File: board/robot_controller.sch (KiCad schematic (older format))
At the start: 3 parts

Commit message: Voltage Regulator, Reset Logic
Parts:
- added C?: 100nF, symbol CAP
- added C? (x2): 2.2uF, symbol C
- added SW?: SPST, symbol SPST
- gave numbers to parts that had none: 3
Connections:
- net at U2.106 (VCAP2): now also C?.2
- net +3.3V: now reaches U2.108 (VDD)
- net +3.3V: now also U2.121 (VDD), U2.131 (VDD), U2.144 (VDD), U2.17 (VDD), U2.30 (VDD), U2.32 (VREF+), U2.33 (VDDA), U2.39 (VDD), U2.52 (VDD), U2.6 (VBAT), U2.62 (VDD), U2.72 (VDD), U2.84 (VDD), U2.95 (VDD)
- net MCU_RESET: now reaches U2.25 (~NRST)
- net MCU_RESET: now also C?.1, SW?.1
- net at U2.71 (VCAP1): now also C?.2
- new net GND: C?.1, C?.1, C?.2, SW?.2
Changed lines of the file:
@@
 $EndDescr
 $Comp
-L STM32F405-144 U?
+L STM32F405-144 U2
 U 1 1 52E41F67
 P 37850 17150
-F 0 "U?" H 36350 13600 60  0000 C CNN
+F 0 "U2" H 36350 13600 60  0000 C CNN
 F 1 "STM32F405-144" H 37850 17150 60  0000 C CNN
 F 2 "" H 35850 14500 60  0000 C CNN
@@
 $EndComp
 $Comp
-L L6470 U?
+L L6470 U1
 U 1 1 52E4501F
 P 3950 4400
-F 0 "U?" H 3300 3450 60  0000 C CNN
+F 0 "U1" H 3300 3450 60  0000 C CNN
 F 1 "L6470" H 3950 4400 60  0000 C CNN
 F 2 "" H 5000 4200 60  0000 C CNN
@@
 $EndComp
 $Comp
-L CONN_STEPPER J?
+L CONN_STEPPER J1
 U 1 1 52E45532
 P 5525 4400
-F 0 "J?" H 5425 4050 60  0000 C CNN
+F 0 "J1" H 5425 4050 60  0000 C CNN
 F 1 "CONN_STEPPER" V 5775 4400 60  0001 C CNN
 F 2 "" H 5075 4200 60  0000 C CNN
@@
 	1    0    0    -1
 $EndComp
+$Comp
+L GND #PWR01
+U 1 1 52E46471
+P 36000 13450
+F 0 "#PWR01" H 36000 13450 30  0001 C CNN
+F 1 "GND" H 36000 13380 30  0001 C CNN
+F 2 "" H 36000 13450 60  0000 C CNN
+F 3 "" H 36000 13450 60  0000 C CNN
+	1    36000 13450
+	1    0    0    -1
+$EndComp
+Connection ~ 36000 13250
+Wire Wire Line
+	36000 13250 36150 13250
+Wire Wire Line
+	36000 12850 36000 13450
+Wire Wire Line
+	36000 12850 36150 12850
+Wire Wire Line
+	36800 12850 36800 13350
+Wire Wire Line
+	36550 12850 36800 12850
+Wire Wire Line
+	36700 13250 36700 13350
+Wire Wire Line
+	36550 13250 36700 13250
+Text Label 38800 13250 1    60   ~ 0
+MCU_RESET
+Wire Wire Line
+	38800 13250 38800 13350
+Wire Wire Line
+	40600 12900 40800 12900
+Text Label 40600 12900 2    60   ~ 0
+MCU_RESET
+$Comp
+L CAP C?
+U 1 1 52E46E20
+P 40700 13250
+F 0 "C?" H 40800 13400 50  0000 C CNN
+F 1 "100nF" H 40850 13100 50  0000 C CNN
+F 2 "" H 40700 13250 60  0000 C CNN
+F 3 "" H 40700 13250 60  0000 C CNN
+	1    40700 13250
+	1    0    0    -1
+$EndComp
+$Comp
+L GND #PWR?
+U 1 1 52E46E34
+P 40700 13600
+F 0 "#PWR?" H 40700 13600 30  0001 C CNN
+F 1 "GND" H 40700 13530 30  0001 C CNN
+F 2 "" H 40700 13600 60  0000 C CNN
+F 3 "" H 40700 13600 60  0000 C CNN
+	1    40700 13600
+	1    0    0    -1
+$EndComp
+Wire Wire Line
+	40700 13500 40700 13600
+Wire Wire Line
+	40700 12900 40700 13000
+$Comp
+L SPST SW?
+U 1 1 52E4700C
+P 41300 12900
+F 0 "SW?" H 41300 13000 70  0000 C CNN
+F 1 "SPST" H 41300 12800 70  0000 C CNN
+F 2 "" H 41300 12900 60  0000 C CNN
+F 3 "" H 41300 12900 60  0000 C CNN
+	1    41300 12900
+	1    0    0    -1
+$EndComp
+Connection ~ 40700 12900
+$Comp
+L GND #PWR?
+U 1 1 52E4704D
+P 41900 13000
+F 0 "#PWR?" H 41900 13000 30  0001 C CNN
+F 1 "GND" H 41900 12930 30  0001 C CNN
+F 2 "" H 41900 13000 60  0000 C CNN
+F 3 "" H 41900 13000 60  0000 C CNN
+	1    41900 13000
+	1    0    0    -1
+$EndComp
+Wire Wire Line
+	41800 12900 41900 12900
+Wire Wire Line
+	41900 12900 41900 13000
+$Comp
+L +3.3V #PWR?
+U 1 1 52E474FF
+P 37000 13150
+F 0 "#PWR?" H 37000 13110 30  0001 C CNN
+F 1 "+3.3V" H 37000 13260 30  0000 C CNN
+F 2 "" H 37000 13150 60  0000 C CNN
+F 3 "" H 37000 13150 60  0000 C CNN
+	1    37000 13150
+	1    0    0    -1
+$EndComp
+Wire Wire Line
+	37000 13150 37000 13350
+Wire Wire Line
+	37000 13250 38600 13250
+Wire Wire Line
+	38600 13250 38600 13350
+Connection ~ 37000 13250
+Wire Wire Line
+	38300 13350 38300 13250
+Connection ~ 38300 13250
+Wire Wire Line
+	38200 13350 38200 13250
+Connection ~ 38200 13250
+Wire Wire Line
+	38100 13350 38100 13250
+Connection ~ 38100 13250
+Wire Wire Line
+	38000 13350 38000 13250
+Connection ~ 38000 13250
+Wire Wire Line
+	37900 13250 37900 13350
+Connection ~ 37900 13250
+Wire Wire Line
+	37800 13250 37800 13350
+Connection ~ 37800 13250
+Wire Wire Line
+	37700 13350 37700 13250
+Connection ~ 37700 13250
+Wire Wire Line
+	37600 13350 37600 13250
+Connection ~ 37600 13250
+Wire Wire Line
+	37500 13350 37500 13250
+Connection ~ 37500 13250
+Wire Wire Line
+	37400 13350 37400 13250
+Connection ~ 37400 13250
+Wire Wire Line
+	37300 13350 37300 13250
+Connection ~ 37300 13250
+Wire Wire Line
+	37200 13250 37200 13350
+Connection ~ 37200 13250
+Wire Wire Line
+	38500 13350 38500 13250
+Connection ~ 38500 13250
+$Comp
+L C C?
+U 1 1 52E477FB
+P 36350 13250
+F 0 "C?" V 36300 13150 50  0000 R CNN
+F 1 "2.2uF" V 36450 13150 50  0000 R CNN
+F 2 "" H 36350 13250 60  0000 C CNN
+F 3 "" H 36350 13250 60  0000 C CNN
+	1    36350 13250
+	0    -1   -1   0
+$EndComp
+$Comp
+L C C?
+U 1 1 52E478D0
+P 36350 12850
+F 0 "C?" V 36300 12750 50  0000 R CNN
+F 1 "2.2uF" V 36450 12750 50  0000 R CNN
+F 2 "" H 36350 12850 60  0000 C CNN
+F 3 "" H 36350 12850 60  0000 C CNN
+	1    36350 12850
+	0    -1   -1   0
+$EndComp
 $EndSCHEMATC

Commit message: Wired up the stepper driver blocks in the main schematic.
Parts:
- removed J1: CONN_STEPPER, symbol CONN_STEPPER
- removed U1: L6470, symbol L6470
- added R?: 1.1k, symbol R
- added R?: 16k, symbol R
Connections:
- net labels added: +24V, 24V_ADC, MISO, MOSI, SCK, STEPPER0-~CS, STEPPER0_~BUSY~/SYNC, STEPPER1-~CS, STEPPER1_~BUSY~/SYNC, STEPPER2-~CS, STEPPER2_~BUSY~/SYNC, STEPPER3-~CS, STEPPER3_~BUSY~/SYNC, STEPPERS_OSCIN, STEPPERS_STCK, STEPPERS_~FLAG, STEPPERS_~RST, STEPPER_OSC
- wire segments 29 -> 77

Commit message: Fixed airwire positions.
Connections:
- net labels added: STEPPERS_OSC_SYNC
- net labels removed: STEPPER_OSC
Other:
- moved on the sheet: R?

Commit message: FTDI USB
I have added USB connectivity to this processor via an FT232RL
interface chip.
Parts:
- removed C?: 100nF, symbol CAP
- removed C? (x2): 2.2uF, symbol C
- added C?: 10nF, symbol C
- added C?: 1uF, symbol C
- added C? (x21): 100nF, symbol C
- added C?: 4.7uF, symbol C
- added C? (x2): 2.2uF, symbol C
- added J?: USB-CONN, symbol USB-CONN
- added R? (x3): 10k, symbol R
- added SW?: SPST, symbol SPST
- added U?: FT232RL, symbol FT232RL
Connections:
- net +3.3V: now also U2.143 (PDRON), C?.1, C?.1, C?.1, C?.1, C?.1, C?.1, C?.1, C?.1, C?.1, C?.1, C?.1, C?.1, C?.1, C?.1, C?.1, C?.1, C?.1, C?.1, C?.1, C?.1, R?.2, SW?.2, U?.4 (VCCIO)
- net GND: now also U2.107 (VSS), U2.120 (VSS), U2.130 (VSS), U2.16 (VSS), U2.31 (VSSA), U2.38 (VSS), U2.51 (VSS), U2.61 (VSS), U2.83 (VSS), U2.94 (VSS), C?.2, C?.2, C?.2, C?.2, C?.2, C?.2, C?.2, C?.2, C?.2, C?.2, C?.2, C?.2, C?.2, C?.2, C?.2, C?.2, C?.2, C?.2, C?.2, C?.2, C?.2, C?.2, C?.2, C?.2, C?.2, C?.2, J?.4 (GND), R?.2, R?.2, U?.18 (GND), U?.21 (GND), U?.25 (AGND), U?.26 (TEST), U?.7 (GND)
- net MCU_RESET: now also C?.1
- net USART1_TX: now reaches U2.101 (PA9)
- net USART1_RX: now reaches U2.102 (PA10)
- net USART1_CTS: now reaches U2.103 (PA11)
- net USART1_RTS: now reaches U2.104 (PA12)
- net VCAP2: now reaches U2.106 (VCAP2)
- net VCAP2: now also C?.1
- net BOOT0: now reaches U2.138 (BOOT0)
- net BOOT0: now also R?.1, SW?.1
- net BOOT1: now reaches U2.47 (PB1)
- net BOOT1: now also R?.1
- net VCAP1: now reaches U2.71 (VCAP1)
- net VCAP1: now also C?.1
- new net: R?.1, U?.14 (CBUS3)
- new net: J?.3 (DP), U?.15 (USBD+)
- new net: J?.2 (DM), U?.16 (USBD-)
- new net: C?.1, U?.17 (3V3OUT)
- new net +5V: C?.1, C?.1, J?.1 (VCC), U?.20 (VCC)
- new net UART1_CTS: U?.3 (RTS)
- new net UART1_RTS: U?.11 (CTS)
- new net UART1_RX: U?.1 (TXD)
- new net UART1_TX: U?.5 (RXD)
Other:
- note added: "Default: Flash Memory"
- note added: "FTDI USB"
- note added: "MCU Analog Decoupling"
- note added: "MCU Boot Address"
- note added: "MCU Digital Decoupling"
- note added: "MCU Regulator Support"
- note added: "MCU Reset"
- note added: "No option to boot from\nSRAM"
- note added: "Pressed: System Memory"
- moved on the sheet: SW?

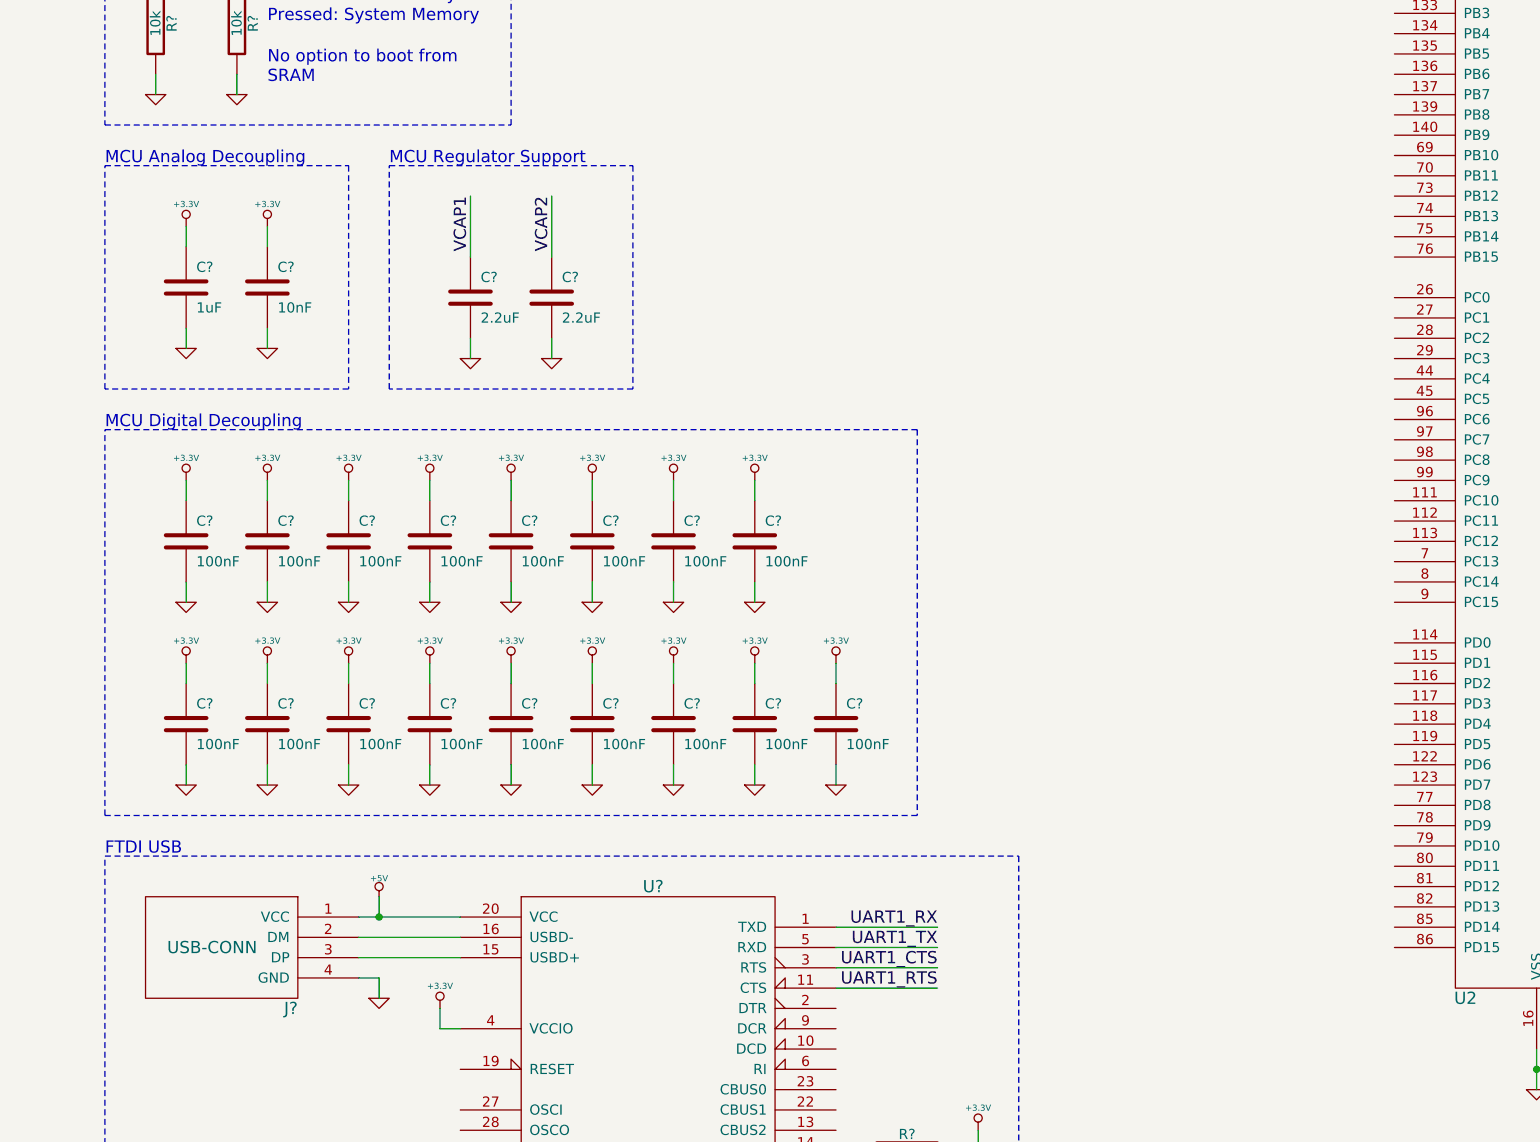
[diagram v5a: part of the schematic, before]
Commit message: Hardware USB
I have added hardware USB support to the board.
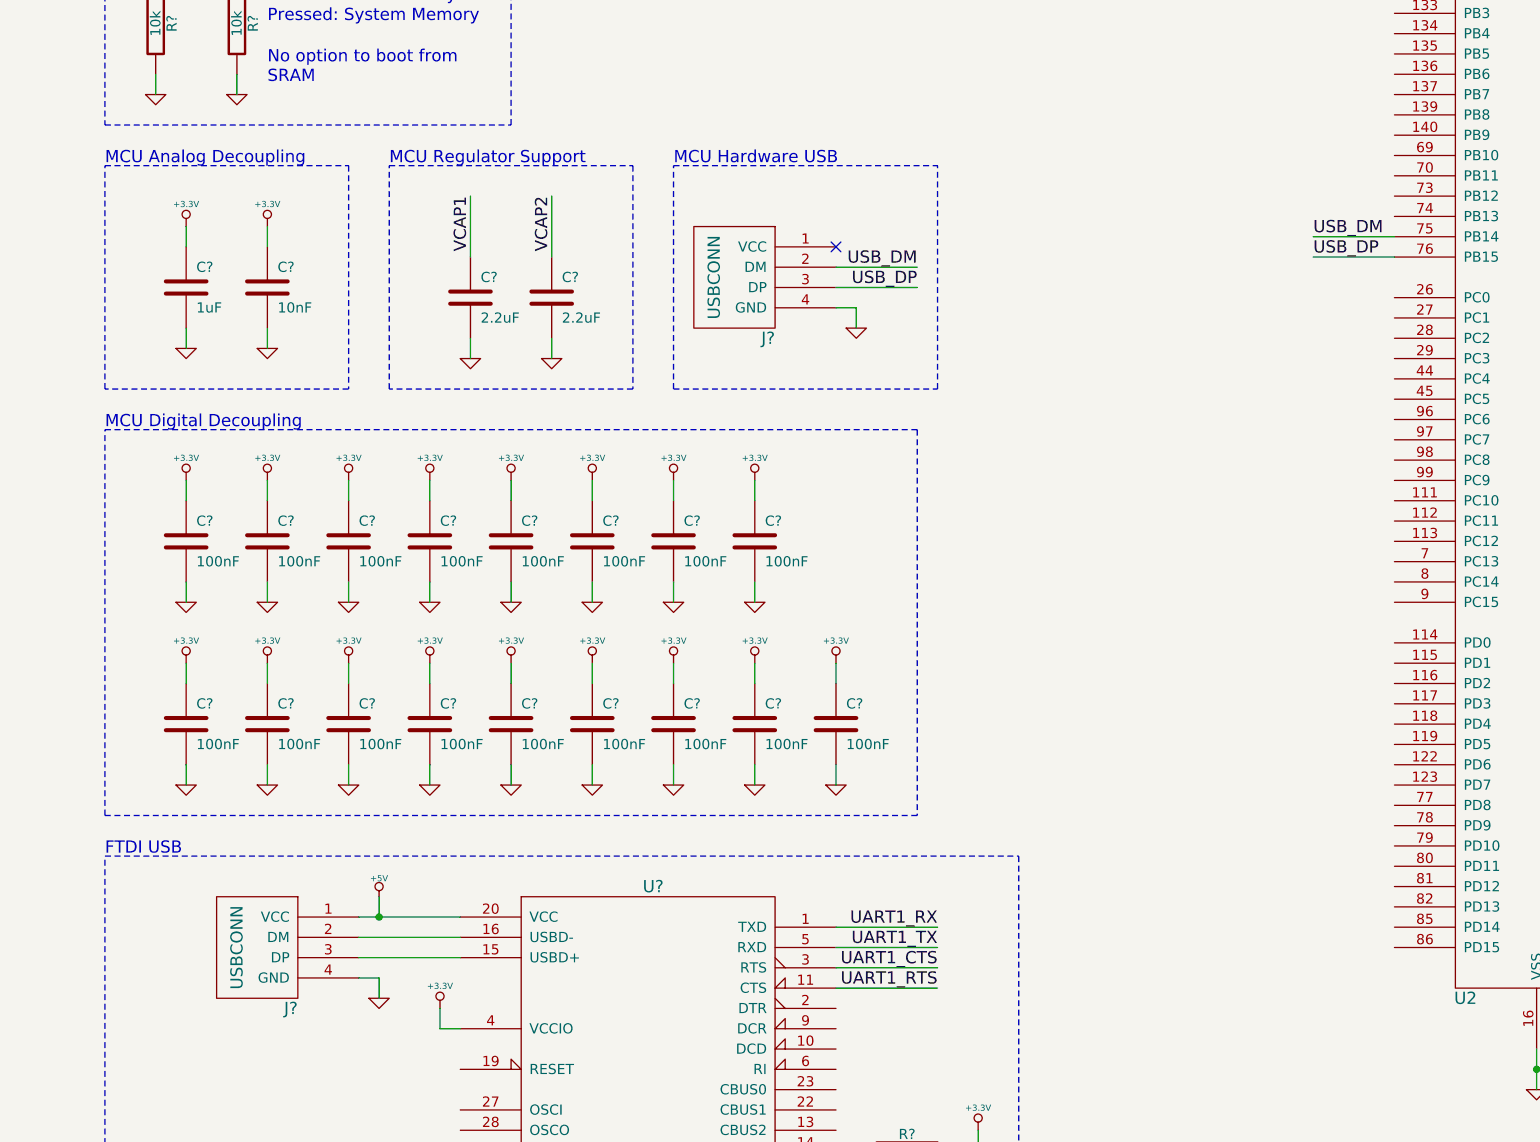
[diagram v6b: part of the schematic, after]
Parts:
- removed J?: USB-CONN, symbol USB-CONN
- added J? (x2): USBCONN, symbol USBCONN
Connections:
- net +5V: now also J?.1 (VCC)
- net GND: now also J?.4 (GND), J?.4 (GND)
- net USB_DM: now reaches U2.75 (PB14)
- net USB_DM: now also J?.2 (DM)
- net USB_DP: now reaches U2.76 (PB15)
- net USB_DP: now also J?.3 (DP)
- net at U?.15 (USBD+): now also J?.3 (DP)
- net at U?.16 (USBD-): now also J?.2 (DM)
- no-connect marks 0 -> 1
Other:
- note added: "MCU Hardware USB"
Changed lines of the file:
@@
 	39000 13150 39000 13350
-$Comp
-L USB-CONN J?
-U 1 1 52F128DD
-P 30300 20450
-F 0 "J?" H 30000 20150 60  0000 L CNN
-F 1 "USB-CONN" H 30200 20450 60  0000 L CNN
-F 2 "" H 30300 20450 60  0000 C CNN
-F 3 "" H 30300 20450 60  0000 C CNN
-	1    30300 20450
-	-1   0    0    -1
-$EndComp
 $Comp
 L GND #PWR?
@@
 Text Label 35400 15050 0    60   ~ 0
 USART1_RTS
+Text Label 35600 16950 0    60   ~ 0
+USB_DM
+Text Label 35600 17050 0    60   ~ 0
+USB_DP
+Wire Wire Line
+	36000 16950 35600 16950
+Wire Wire Line
+	36000 17050 35600 17050
+Text Notes 32450 16600 0    60   ~ 0
+MCU Hardware USB
+Wire Notes Line
+	32450 16600 33750 16600
+Wire Notes Line
+	33750 17700 33750 16600
+Wire Notes Line
+	32450 17700 33750 17700
+Wire Notes Line
+	32450 17700 32450 16600
+$Comp
+L USBCONN J?
+U 1 1 52EF0DB4
+P 30300 20450
+F 0 "J?" H 30000 20150 60  0000 L CNN
+F 1 "USBCONN" V 30300 20450 60  0000 C CNN
+F 2 "" H 30300 20450 60  0000 C CNN
+F 3 "" H 30300 20450 60  0000 C CNN
+	1    30300 20450
+	-1   0    0    -1
+$EndComp
+$Comp
+L USBCONN J?
+U 1 1 52EF237D
+P 32650 17150
+F 0 "J?" H 32350 16850 60  0000 L CNN
+F 1 "USBCONN" V 32650 17150 60  0000 C CNN
+F 2 "" H 32650 17150 60  0000 C CNN
+F 3 "" H 32650 17150 60  0000 C CNN
+	1    32650 17150
+	-1   0    0    -1
+$EndComp
+$Comp
+L GND #PWR?
+U 1 1 52EF281B
+P 33350 17400
+F 0 "#PWR?" H 33350 17400 30  0001 C CNN
+F 1 "GND" H 33350 17330 30  0001 C CNN
+F 2 "" H 33350 17400 60  0000 C CNN
+F 3 "" H 33350 17400 60  0000 C CNN
+	1    33350 17400
+	1    0    0    -1
+$EndComp
+Wire Wire Line
+	33350 17300 33350 17400
+Wire Wire Line
+	33250 17300 33350 17300
+NoConn ~ 33250 17000
+Wire Wire Line
+	33250 17100 33650 17100
+Wire Wire Line
+	33250 17200 33650 17200
+Text Label 33650 17100 2    60   ~ 0
+USB_DM
+Text Label 33650 17200 2    60   ~ 0
+USB_DP
 $EndSCHEMATC
